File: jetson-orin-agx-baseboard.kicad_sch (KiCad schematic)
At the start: 0 parts

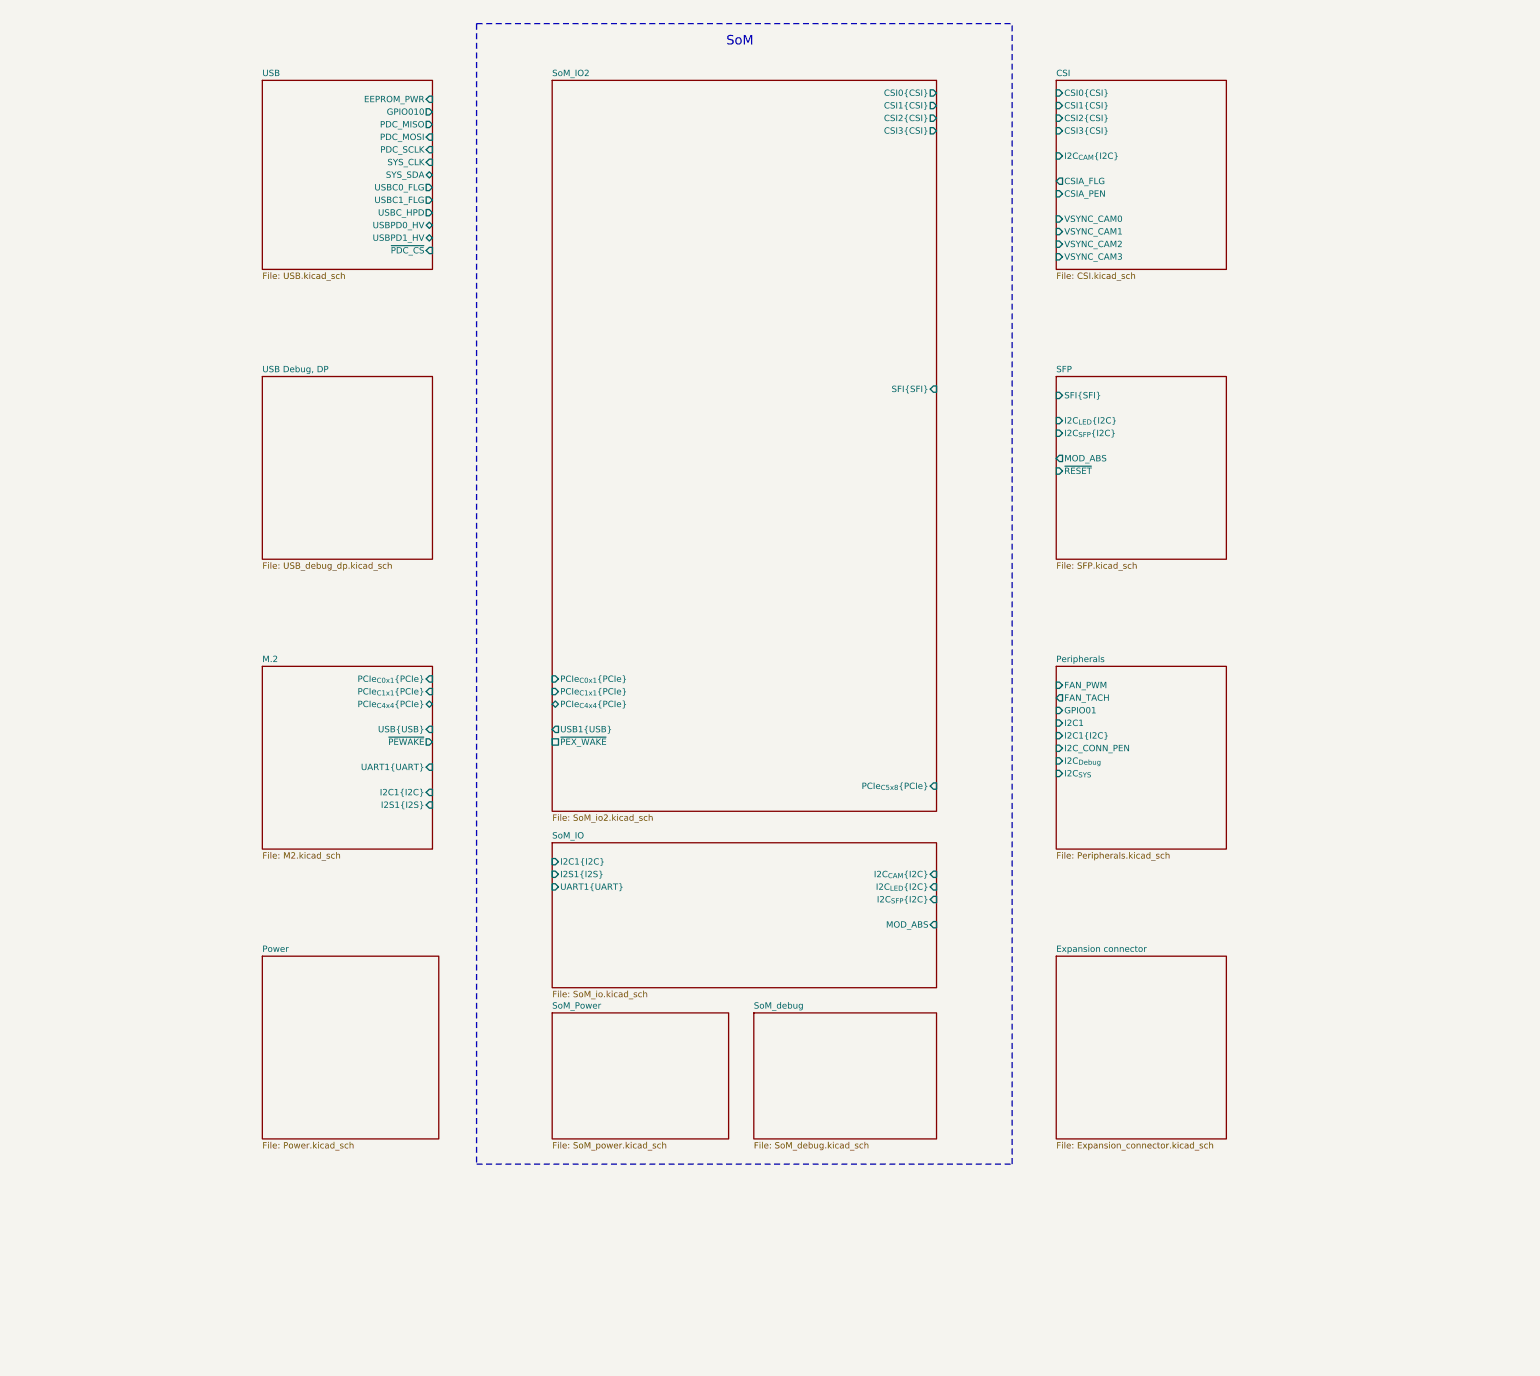
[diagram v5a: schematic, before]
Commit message: [#81970] Start routing main peripherals on root schematic
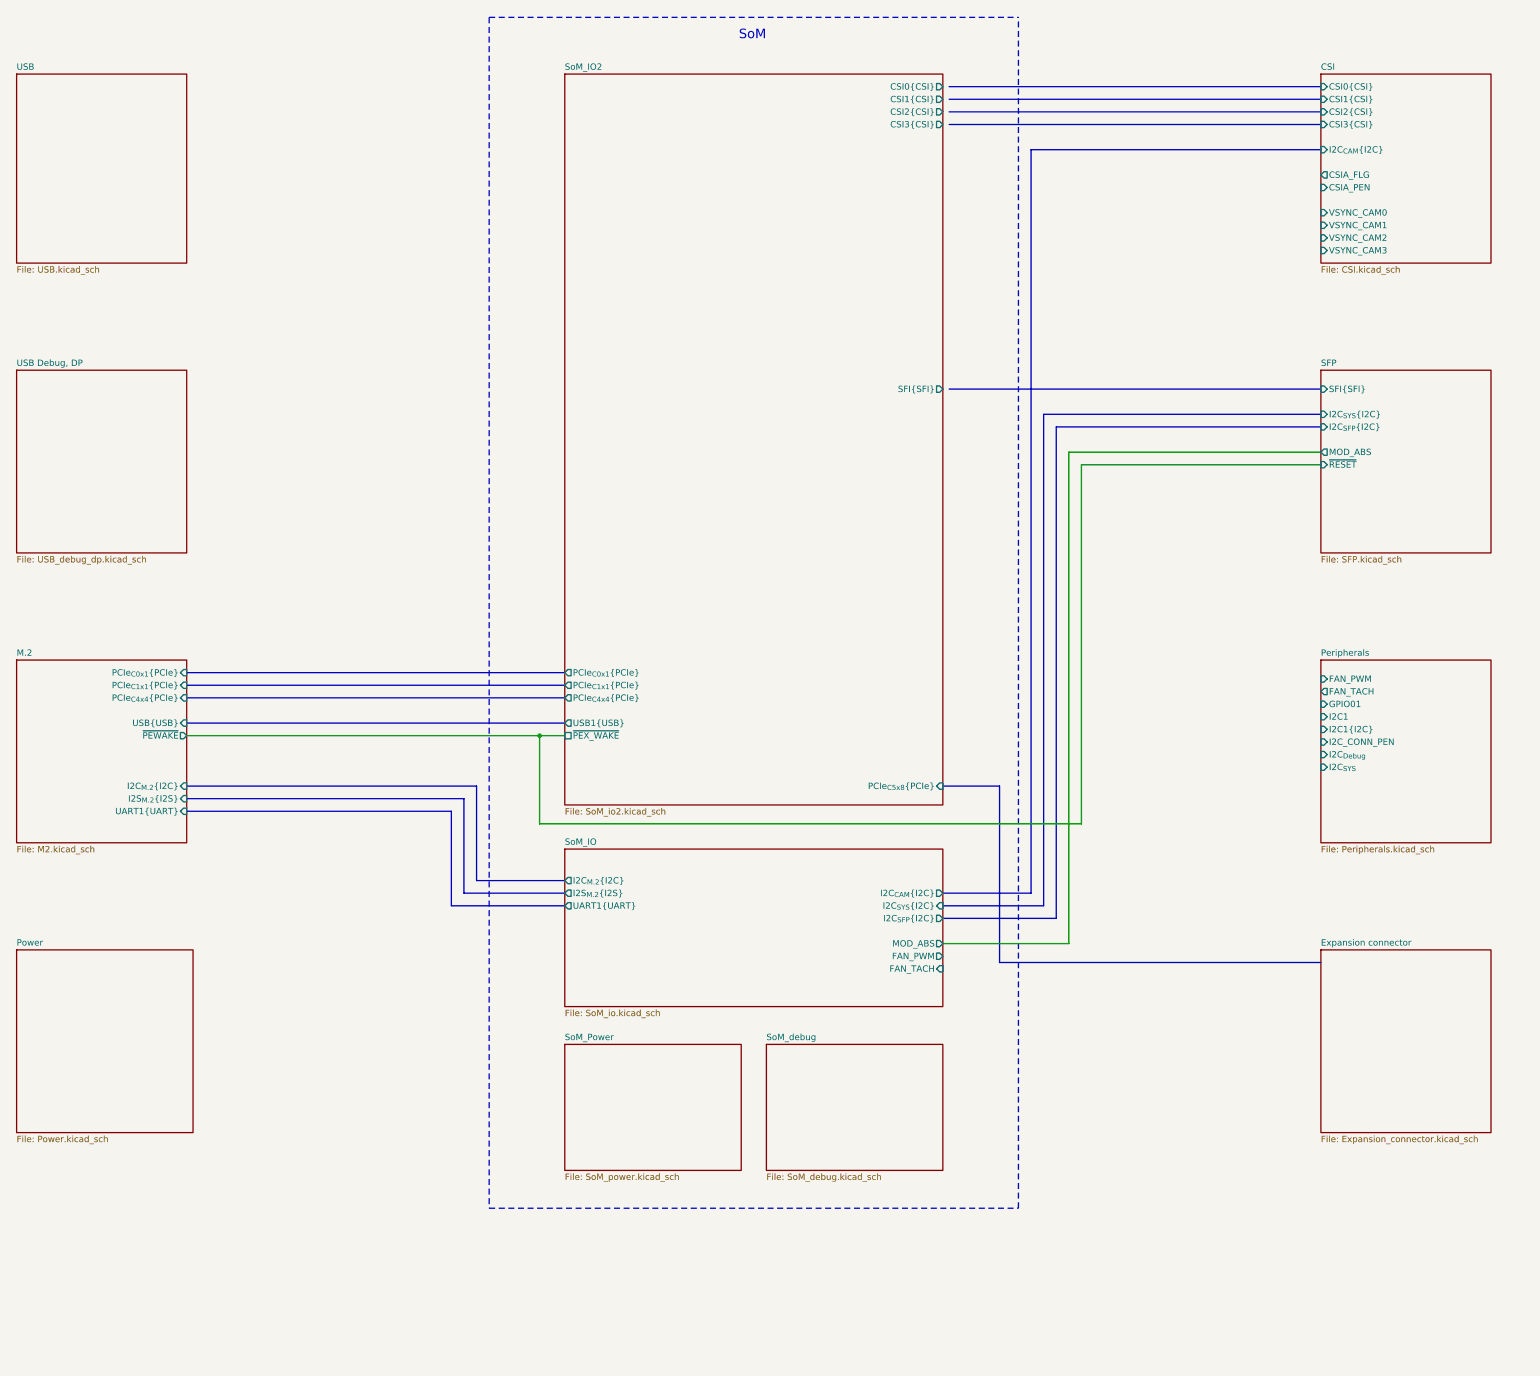
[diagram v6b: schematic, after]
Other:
- sheet M.2 ports: added I2C_{M.2}{I2C}, I2S_{M.2}{I2S}; removed I2C1{I2C}, I2S1{I2S}
- sheet SFP ports: added I2C_{SYS}{I2C}; removed I2C_{LED}{I2C}
- sheet SoM_IO ports: added FAN_PWM, FAN_TACH, I2C_{M.2}{I2C}, I2C_{SYS}{I2C}, I2S_{M.2}{I2S}; removed I2C1{I2C}, I2C_{LED}{I2C}, I2S1{I2S}
- sheet USB ports: added none; removed EEPROM_PWR, GPIO010, PDC_MISO, PDC_MOSI, PDC_SCLK, SYS_CLK, SYS_SDA, USBC0_FLG, USBC1_FLG, USBC_HPD, USBPD0_HV, USBPD1_HV, ~{PDC_CS}

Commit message: [#81970] Route GPIO pins from CSI and peripheral sheets on root schematic
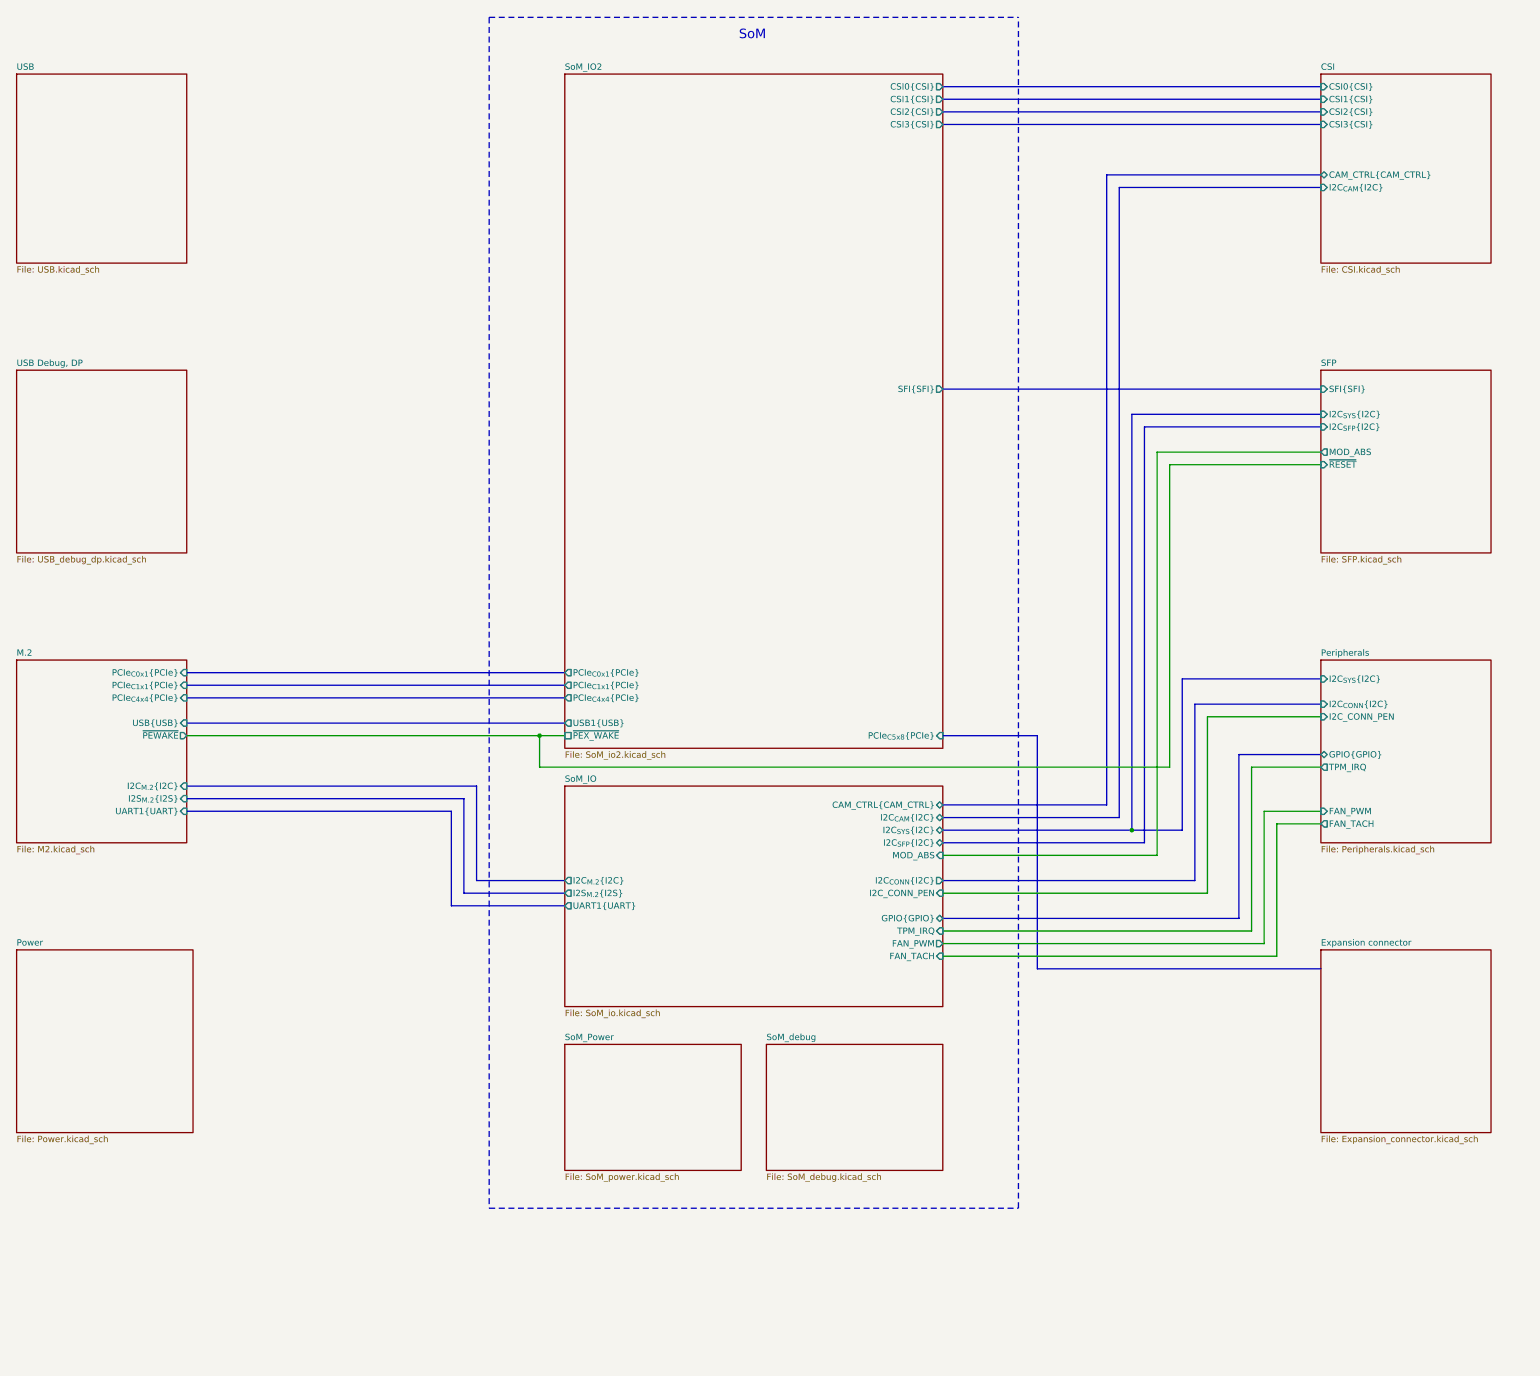
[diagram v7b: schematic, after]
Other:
- sheet CSI ports: added CAM_CTRL{CAM_CTRL}; removed CSIA_FLG, CSIA_PEN, VSYNC_CAM0, VSYNC_CAM1, VSYNC_CAM2, VSYNC_CAM3
- sheet Peripherals ports: added GPIO{GPIO}, I2C_{CONN}{I2C}, I2C_{SYS}{I2C}, TPM_IRQ; removed GPIO01, I2C1, I2C1{I2C}, I2C_{Debug}, I2C_{SYS}
- sheet SoM_IO ports: added CAM_CTRL{CAM_CTRL}, GPIO{GPIO}, I2C_CONN_PEN, I2C_{CONN}{I2C}, TPM_IRQ; removed none

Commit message: [#81970] Reorganise schematic layout to clean up routing
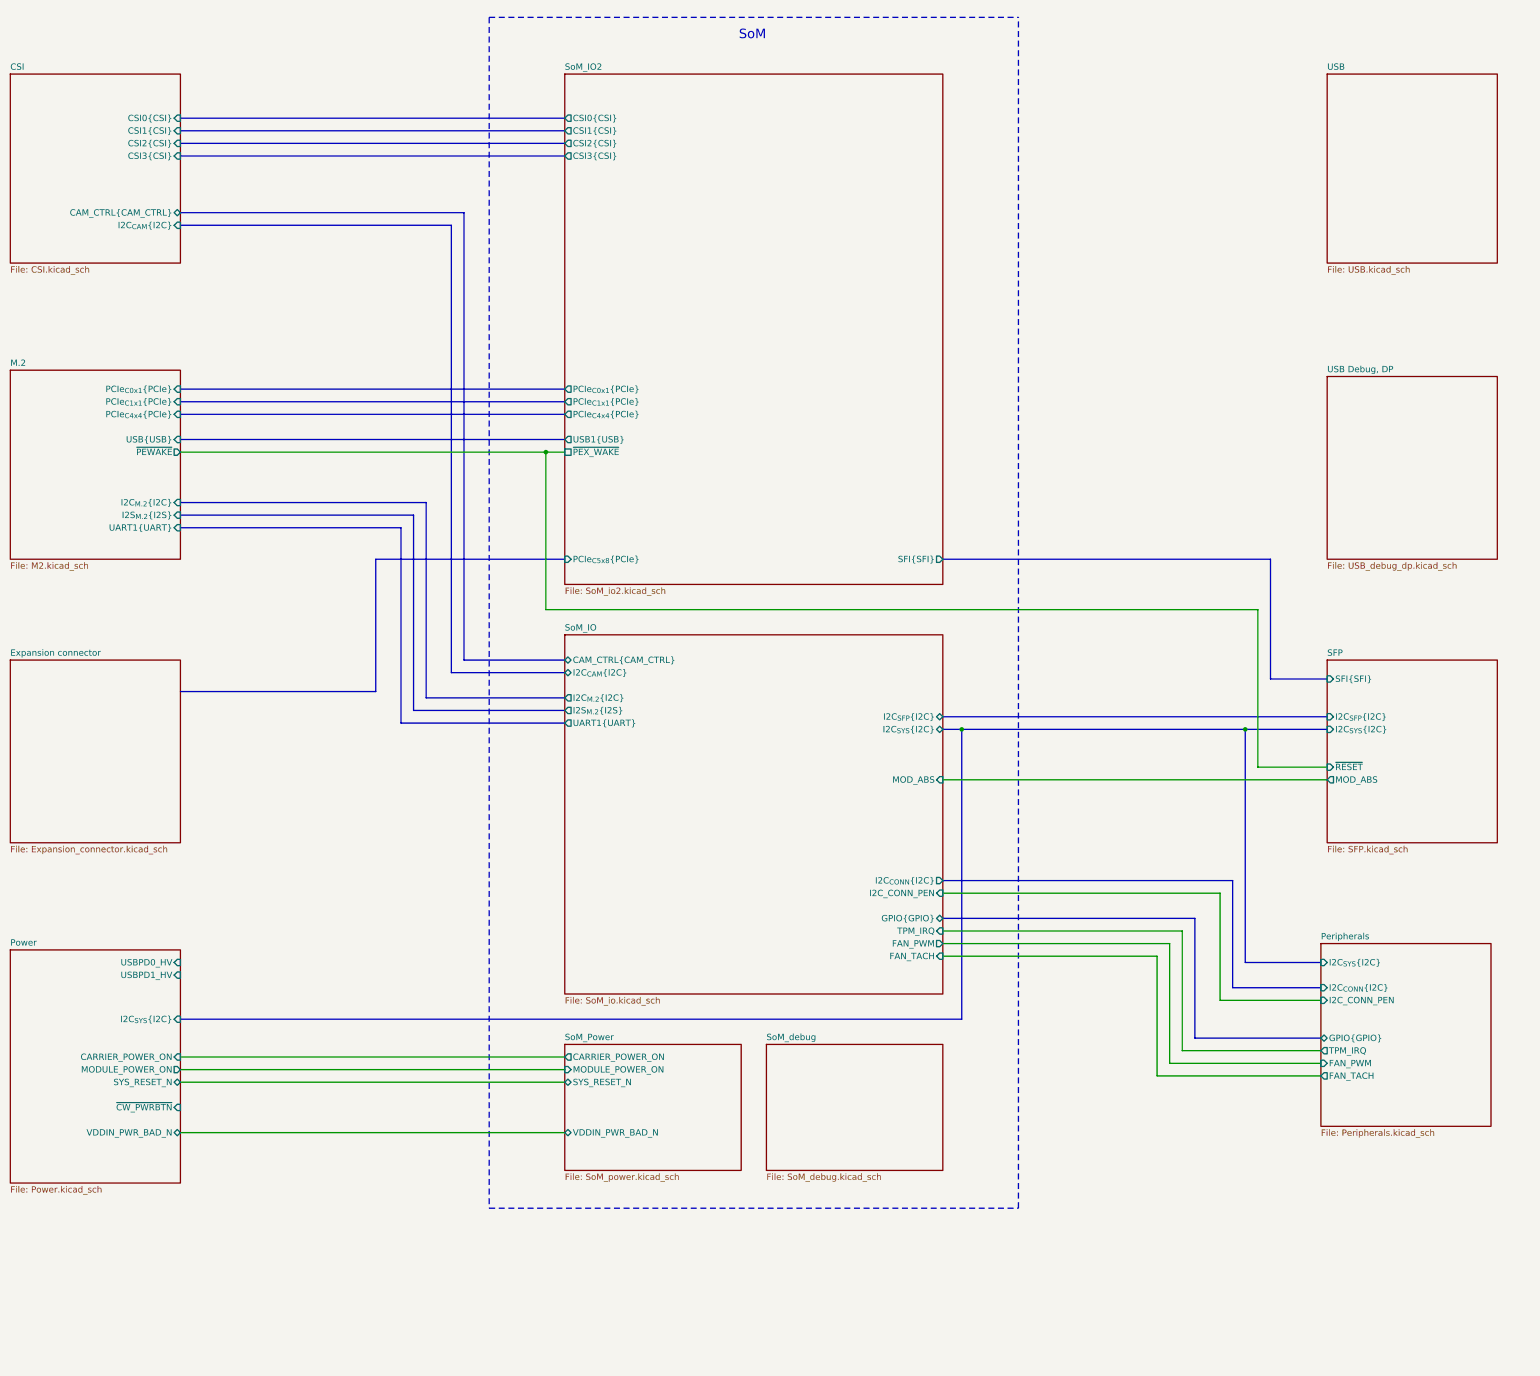
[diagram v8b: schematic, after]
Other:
- sheet Power ports: added CARRIER_POWER_ON, I2C_{SYS}{I2C}, MODULE_POWER_ON, SYS_RESET_N, USBPD0_HV, USBPD1_HV, VDDIN_PWR_BAD_N, ~{CW_PWRBTN}; removed none
- sheet SoM_Power ports: added CARRIER_POWER_ON, MODULE_POWER_ON, SYS_RESET_N, VDDIN_PWR_BAD_N; removed none
